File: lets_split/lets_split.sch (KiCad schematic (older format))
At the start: 60 parts, among them J1 3PIN, J2 6PIN, J3 3PIN, SW1 SW_PUSH, SW10 SW_PUSH, SW11 SW_PUSH, SW12 SW_PUSH, SW13 SW_PUSH, SW14 SW_PUSH, SW15 SW_PUSH, SW16 SW_PUSH, SW17 SW_PUSH, SW18 SW_PUSH, SW19 SW_PUSH, SW2 SW_PUSH, SW20 SW_PUSH, SW21 SW_PUSH, SW22 SW_PUSH, SW23 SW_PUSH, SW24 SW_PUSH, SW3 SW_PUSH, SW4 SW_PUSH, SW5 SW_PUSH, SW6 SW_PUSH, SW7 SW_PUSH, SW8 SW_PUSH, SW9 SW_PUSH, U1 TEENSY2.0, U2 HOLE, U3 HOLE, U4 HOLE, U5 HOLE

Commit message: Changed to use kailh sockets, start of branch
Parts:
- removed U2, U3, U4, U5: HOLE, prettylib:HOLE, symbol HOLE
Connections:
- wire segments 24 -> 57
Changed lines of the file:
@@
 LIBS:contrib
 LIBS:valves
-LIBS:component
 LIBS:lets_split-cache
 EELAYER 25 0
@@
 $EndComp
 Wire Wire Line
-	5750 2500 9450 2500
+	5750 2500 6500 2500
+Wire Wire Line
+	6500 2500 7200 2500
+Wire Wire Line
+	7200 2500 7950 2500
+Wire Wire Line
+	7950 2500 8700 2500
+Wire Wire Line
+	8700 2500 9450 2500
 Connection ~ 8700 2500
 Connection ~ 7950 2500
@@
 $EndComp
 Wire Wire Line
-	5750 3000 9450 3000
+	5750 3000 6500 3000
+Wire Wire Line
+	6500 3000 7200 3000
+Wire Wire Line
+	7200 3000 7950 3000
+Wire Wire Line
+	7950 3000 8700 3000
+Wire Wire Line
+	8700 3000 9450 3000
 Connection ~ 8700 3000
 Connection ~ 7950 3000
@@
 $EndComp
 Wire Wire Line
-	5750 3500 9450 3500
+	5750 3500 6500 3500
+Wire Wire Line
+	6500 3500 7200 3500
+Wire Wire Line
+	7200 3500 7950 3500
+Wire Wire Line
+	7950 3500 8700 3500
+Wire Wire Line
+	8700 3500 9450 3500
 Connection ~ 8700 3500
 Connection ~ 7950 3500
@@
 $EndComp
 Wire Wire Line
-	5750 4000 9450 4000
+	5750 4000 6500 4000
+Wire Wire Line
+	6500 4000 7200 4000
+Wire Wire Line
+	7200 4000 7950 4000
+Wire Wire Line
+	7950 4000 8700 4000
+Wire Wire Line
+	8700 4000 9450 4000
 Connection ~ 8700 4000
 Connection ~ 7950 4000
@@
 Connection ~ 6500 4000
 Wire Wire Line
-	5150 2200 5150 3700
+	5150 2200 5150 2700
+Wire Wire Line
+	5150 2700 5150 3200
+Wire Wire Line
+	5150 3200 5150 3700
 Connection ~ 5150 2700
 Connection ~ 5150 3200
 Wire Wire Line
-	5900 2200 5900 3700
+	5900 2200 5900 2700
+Wire Wire Line
+	5900 2700 5900 3200
+Wire Wire Line
+	5900 3200 5900 3700
 Connection ~ 5900 2700
 Connection ~ 5900 3200
 Wire Wire Line
-	6600 2200 6600 3700
+	6600 2200 6600 2700
+Wire Wire Line
+	6600 2700 6600 3200
+Wire Wire Line
+	6600 3200 6600 3700
 Connection ~ 6600 3200
 Connection ~ 6600 2700
 Wire Wire Line
-	7350 2200 7350 3700
+	7350 2200 7350 2700
+Wire Wire Line
+	7350 2700 7350 3200
+Wire Wire Line
+	7350 3200 7350 3700
 Connection ~ 7350 2700
 Connection ~ 7350 3200
 Wire Wire Line
-	8100 2200 8100 3700
+	8100 2200 8100 2700
+Wire Wire Line
+	8100 2700 8100 3200
+Wire Wire Line
+	8100 3200 8100 3700
 Connection ~ 8100 3200
 Connection ~ 8100 2700
 Wire Wire Line
-	8850 2200 8850 3700
+	8850 2200 8850 2700
+Wire Wire Line
+	8850 2700 8850 3200
+Wire Wire Line
+	8850 3200 8850 3700
 Connection ~ 8850 2700
 Connection ~ 8850 3200
@@
 Text GLabel 2600 4150 2    60   Input ~ 0
 data
-Text GLabel 6450 950  1    60   Input ~ 0
+Text GLabel 6500 900  1    55   Input ~ 0
 data
 $Comp
 L R R2
 U 1 1 57D4D4E2
-P 6300 950
-F 0 "R2" V 6380 950 50  0000 C CNN
-F 1 "R" V 6300 950 50  0000 C CNN
-F 2 "footprint:RESISTOR" V 6230 950 50  0001 C CNN
-F 3 "" H 6300 950 50  0000 C CNN
-	1    6300 950
+P 6250 950
+F 0 "R2" V 6330 950 50  0000 C CNN
+F 1 "R" V 6250 950 50  0000 C CNN
+F 2 "footprint:RESISTOR" V 6180 950 50  0001 C CNN
+F 3 "" H 6250 950 50  0000 C CNN
+	1    6250 950
 	0    1    1    0
 $EndComp
 Wire Wire Line
-	6450 950  6500 1450
-Wire Wire Line
-	6450 950  6900 950
+	6500 900  6500 950
+Wire Wire Line
+	6500 950  6500 1450
+Wire Wire Line
+	6400 950  6500 950
+Wire Wire Line
+	6500 950  6900 950
 Wire Wire Line
 	6900 950  6900 1450
-Connection ~ 6900 950
-Connection ~ 6450 950
+Connection ~ 6500 950
 Wire Wire Line
 	6800 1450 6800 1350
@@
 	6800 1350 6600 1350
 Wire Wire Line
+	6600 900  6600 1350
+Wire Wire Line
 	6600 1350 6600 1450
-Connection ~ 6800 1350
 Connection ~ 6600 1350
-Text GLabel 6600 1350 1    60   Input ~ 0
+Text GLabel 6600 900  1    55   Input ~ 0
 xtradata
 $Comp
@@
 Text GLabel 7950 950  0    60   Input ~ 0
 xtradata
-Text GLabel 4200 900  0    60   Input ~ 0
+Text GLabel 3625 3550 2    60   Input ~ 0
 xtradata
 $Comp
 L TEST W1
 U 1 1 57D52188
-P 4400 900
-F 0 "W1" H 4400 960 50  0000 C CNN
-F 1 "TEST" H 4400 830 50  0000 C CNN
-F 2 "prettylib:JUMPER_SMD_2DUB" H 4400 900 50  0001 C CNN
-F 3 "" H 4400 900 50  0000 C CNN
-	1    4400 900
-	1    0    0    -1
+P 3425 3550
+F 0 "W1" H 3425 3610 50  0000 C CNN
+F 1 "TEST" H 3425 3480 50  0000 C CNN
+F 2 "prettylib:JUMPER_SMD_2DUB" H 3425 3550 50  0001 C CNN
+F 3 "" H 3425 3550 50  0000 C CNN
+	1    3425 3550
+	-1   0    0    -1
 $EndComp
 $Comp
 L R R1
 U 1 1 57D527EC
-P 4600 750
-F 0 "R1" V 4680 750 50  0000 C CNN
-F 1 "R" V 4600 750 50  0000 C CNN
-F 2 "footprint:RESISTOR" V 4530 750 50  0001 C CNN
-F 3 "" H 4600 750 50  0000 C CNN
-	1    4600 750
+P 3175 3350
+F 0 "R1" V 3255 3350 50  0000 C CNN
+F 1 "R" V 3175 3350 50  0000 C CNN
+F 2 "footprint:RESISTOR" V 3105 3350 50  0001 C CNN
+F 3 "" H 3175 3350 50  0000 C CNN
+	1    3175 3350
 	1    0    0    -1
 $EndComp
@@
 L VCC #PWR05
 U 1 1 57D5288F
-P 6150 950
-F 0 "#PWR05" H 6150 800 50  0001 C CNN
-F 1 "VCC" H 6150 1100 50  0000 C CNN
-F 2 "" H 6150 950 50  0000 C CNN
-F 3 "" H 6150 950 50  0000 C CNN
-	1    6150 950
+P 6100 950
+F 0 "#PWR05" H 6100 800 50  0001 C CNN
+F 1 "VCC" H 6100 1100 50  0000 C CNN
+F 2 "" H 6100 950 50  0000 C CNN
+F 3 "" H 6100 950 50  0000 C CNN
+	1    6100 950
 	1    0    0    -1
 $EndComp
@@
 L VCC #PWR06
 U 1 1 57D52913
-P 4600 600
-F 0 "#PWR06" H 4600 450 50  0001 C CNN
-F 1 "VCC" H 4600 750 50  0000 C CNN
-F 2 "" H 4600 600 50  0000 C CNN
-F 3 "" H 4600 600 50  0000 C CNN
-	1    4600 600
+P 3175 3200
+F 0 "#PWR06" H 3175 3050 50  0001 C CNN
+F 1 "VCC" H 3175 3350 50  0000 C CNN
+F 2 "" H 3175 3200 50  0000 C CNN
+F 3 "" H 3175 3200 50  0000 C CNN
+	1    3175 3200
 	0    1    1    0
 $EndComp
 Wire Wire Line
-	4600 900  4600 4050
-Wire Wire Line
-	4600 4050 2600 4050
+	3175 3500 3175 3550
+Wire Wire Line
+	3175 3550 3175 4050
+Wire Wire Line
+	3175 4050 2600 4050
 Text GLabel 2600 2750 2    60   Input ~ 0
 col0
@@
 Text GLabel 5750 4000 0    60   Input ~ 0
 row3
-$Comp
-L HOLE U2
-U 1 1 57D4E136
-P 1950 6500
-F 0 "U2" H 1950 6500 60  0000 C CNN
-F 1 "HOLE" H 1950 6500 60  0000 C CNN
-F 2 "prettylib:HOLE" H 1950 6500 60  0001 C CNN
-F 3 "" H 1950 6500 60  0000 C CNN
-	1    1950 6500
-	1    0    0    -1
-$EndComp
-$Comp
-L HOLE U3
-U 1 1 57D4E261
-P 4050 6500
-F 0 "U3" H 4050 6500 60  0000 C CNN
-F 1 "HOLE" H 4050 6500 60  0000 C CNN
-F 2 "prettylib:HOLE" H 4050 6500 60  0001 C CNN
-F 3 "" H 4050 6500 60  0000 C CNN
-	1    4050 6500
-	1    0    0    -1
-$EndComp
-$Comp
-L HOLE U4
-U 1 1 57D4E2F6
-P 6050 5650
-F 0 "U4" H 6050 5650 60  0000 C CNN
-F 1 "HOLE" H 6050 5650 60  0000 C CNN
-F 2 "prettylib:HOLE" H 6050 5650 60  0001 C CNN
-F 3 "" H 6050 5650 60  0000 C CNN
-	1    6050 5650
-	1    0    0    -1
-$EndComp
-$Comp
-L HOLE U5
-U 1 1 57D4E38F
-P 8600 5650
-F 0 "U5" H 8600 5650 60  0000 C CNN
-F 1 "HOLE" H 8600 5650 60  0000 C CNN
-F 2 "prettylib:HOLE" H 8600 5650 60  0001 C CNN
-F 3 "" H 8600 5650 60  0000 C CNN
-	1    8600 5650
-	1    0    0    -1
-$EndComp
+Wire Wire Line
+	3225 3550 3175 3550
+Connection ~ 3175 3550
 $EndSCHEMATC

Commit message: Finished desing
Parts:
- removed J2: 6PIN, footprint:4pin35mmAudio, symbol 6PIN
- removed R1, R2: R, footprint:RESISTOR, symbol R
- removed U1: TEENSY2.0, footprint:TEENSY_2.0, symbol TEENSY2.0
- removed W1: TEST, prettylib:JUMPER_SMD_2DUB, symbol TEST
- removed W2: TEST_1P, Wire_Pads:SolderWirePad_single_2mmDrill, symbol TEST_1P
- added J2: CONN_01X04, Connectors:4ucon-20153, symbol CONN_01X04
- added JP1: I2C / Serial, Jumpers:Solder-jumper-NO, symbol JUMPER
- added R1, R2: 4k7, Resistors_ThroughHole:R_Axial_DIN0207_L6.3mm_D2.5mm_P10.16mm_Horizontal, symbol R_Small
- added U1: ArduinoProMicro, plug-in-modules:ArduinoProMicro, symbol ArduinoProMicro
- J1, J3: footprint prettylib:jumper -> Jumpers:jumper-3pin-smd-dualside
- SW1, SW24: footprint flipalps:MXALPS_FLIP -> CherryMX:Kailh-socket
- SW10: renamed from SW14; footprint flipalps:MXALPS_FLIP -> CherryMX:Kailh-socket
- SW11: renamed from SW18; footprint flipalps:MXALPS_FLIP -> CherryMX:Kailh-socket
- SW12: renamed from SW22; footprint flipalps:MXALPS_FLIP -> CherryMX:Kailh-socket
- SW13: renamed from SW3; footprint flipalps:MXALPS_FLIP -> CherryMX:Kailh-socket
- SW14: renamed from SW7; footprint flipalps:MXALPS_FLIP -> CherryMX:Kailh-socket
- SW15: renamed from SW11; footprint flipalps:MXALPS_FLIP -> CherryMX:Kailh-socket
- SW16: renamed from SW15; footprint flipalps:MXALPS_FLIP -> CherryMX:Kailh-socket
- SW17: renamed from SW19; footprint flipalps:MXALPS_FLIP -> CherryMX:Kailh-socket
- SW18: renamed from SW23; footprint flipalps:MXALPS_FLIP -> CherryMX:Kailh-socket
- SW19: renamed from SW4; footprint flipalps:MXALPS_FLIP -> CherryMX:Kailh-socket
- SW2: renamed from SW5; footprint flipalps:MXALPS_FLIP -> CherryMX:Kailh-socket
- SW20: renamed from SW8; footprint flipalps:MXALPS_FLIP -> CherryMX:Kailh-socket
- SW21: renamed from SW12; footprint flipalps:MXALPS_FLIP -> CherryMX:Kailh-socket
- SW22: renamed from SW16; footprint flipalps:MXALPS_FLIP -> CherryMX:Kailh-socket
- SW23: renamed from SW20; footprint flipalps:MXALPS_FLIP -> CherryMX:Kailh-socket
- SW3: renamed from SW9; footprint flipalps:MXALPS_FLIP -> CherryMX:Kailh-socket
- SW4: renamed from SW13; footprint flipalps:MXALPS_FLIP -> CherryMX:Kailh-socket
- SW5: renamed from SW17; footprint flipalps:MXALPS_FLIP -> CherryMX:Kailh-socket
- SW6: renamed from SW21; footprint flipalps:MXALPS_FLIP -> CherryMX:Kailh-socket
- SW7: renamed from SW2; footprint flipalps:MXALPS_FLIP -> CherryMX:Kailh-socket
- SW8: renamed from SW6; footprint flipalps:MXALPS_FLIP -> CherryMX:Kailh-socket
- SW9: renamed from SW10; footprint flipalps:MXALPS_FLIP -> CherryMX:Kailh-socket
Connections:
- net labels added: SCL/D3, SDA
- net labels removed: data, xtradata
- wire segments 57 -> 30

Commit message: Moved panel files into subfolder
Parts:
- removed J1, J3: 3PIN, Jumpers:jumper-3pin-smd-dualside, symbol 3PIN
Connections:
- wire segments 30 -> 61
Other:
- moved on the sheet: J2
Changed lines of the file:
@@
-$EndComp
-$Comp
-L 3PIN J1
-U 1 1 57D4A05A
-P 5750 1700
-F 0 "J1" H 5700 1900 60  0000 C CNN
-F 1 "3PIN" H 5700 1500 60  0000 C CNN
-F 2 "Jumpers:jumper-3pin-smd-dualside" H 5750 1700 60  0001 C CNN
-F 3 "" H 5750 1700 60  0000 C CNN
-	1    5750 1700
-	0    -1   -1   0
-$EndComp
-$Comp
-L 3PIN J3
-U 1 1 57D4A13F
-P 7450 1700
-F 0 "J3" H 7400 1900 60  0000 C CNN
-F 1 "3PIN" H 7400 1500 60  0000 C CNN
-F 2 "Jumpers:jumper-3pin-smd-dualside" H 7450 1700 60  0001 C CNN
-F 3 "" H 7450 1700 60  0000 C CNN
-	1    7450 1700
-	0    -1   -1   0
 $EndComp
 $Comp
 L VCC #PWR01
 U 1 1 57D4A6E4
-P 7550 1500
-F 0 "#PWR01" H 7550 1350 50  0001 C CNN
-F 1 "VCC" H 7550 1650 50  0000 C CNN
-F 2 "" H 7550 1500 50  0000 C CNN
-F 3 "" H 7550 1500 50  0000 C CNN
-	1    7550 1500
-	1    0    0    -1
-$EndComp
-$Comp
-L VCC #PWR02
-U 1 1 57D4A760
-P 5850 1500
-F 0 "#PWR02" H 5850 1350 50  0001 C CNN
-F 1 "VCC" H 5850 1650 50  0000 C CNN
-F 2 "" H 5850 1500 50  0000 C CNN
-F 3 "" H 5850 1500 50  0000 C CNN
-	1    5850 1500
-	1    0    0    -1
-$EndComp
-$Comp
-L GND #PWR03
+P 5850 1325
+F 0 "#PWR01" H 5850 1175 50  0001 C CNN
+F 1 "VCC" H 5850 1475 50  0000 C CNN
+F 2 "" H 5850 1325 50  0000 C CNN
+F 3 "" H 5850 1325 50  0000 C CNN
+	1    5850 1325
+	1    0    0    -1
+$EndComp
+$Comp
+L GND #PWR02
 U 1 1 57D4A7DC
-P 5650 1500
-F 0 "#PWR03" H 5650 1250 50  0001 C CNN
-F 1 "GND" H 5650 1350 50  0000 C CNN
-F 2 "" H 5650 1500 50  0000 C CNN
-F 3 "" H 5650 1500 50  0000 C CNN
-	1    5650 1500
-	-1   0    0    1
-$EndComp
-$Comp
-L GND #PWR04
-U 1 1 57D4A858
-P 7350 1500
-F 0 "#PWR04" H 7350 1250 50  0001 C CNN
-F 1 "GND" H 7350 1350 50  0000 C CNN
-F 2 "" H 7350 1500 50  0000 C CNN
-F 3 "" H 7350 1500 50  0000 C CNN
-	1    7350 1500
-	-1   0    0    1
+P 6325 1525
+F 0 "#PWR02" H 6325 1275 50  0001 C CNN
+F 1 "GND" H 6325 1375 50  0000 C CNN
+F 2 "" H 6325 1525 50  0000 C CNN
+F 3 "" H 6325 1525 50  0000 C CNN
+	1    6325 1525
+	1    0    0    -1
 $EndComp
 Text GLabel 2350 2375 2    55   Input ~ 0
@@
 row0
 $Comp
-L VCC #PWR05
+L VCC #PWR03
 U 1 1 57D5E2B3
 P 1400 1900
-F 0 "#PWR05" H 1400 1750 50  0001 C CNN
+F 0 "#PWR03" H 1400 1750 50  0001 C CNN
 F 1 "VCC" H 1400 2050 50  0000 C CNN
 F 2 "" H 1400 1900 50  0000 C CNN
@@
 $EndComp
 $Comp
-L GND #PWR06
+L GND #PWR04
 U 1 1 57D5FCCF
 P 1400 3050
-F 0 "#PWR06" H 1400 2800 50  0001 C CNN
+F 0 "#PWR04" H 1400 2800 50  0001 C CNN
 F 1 "GND" H 1400 2900 50  0000 C CNN
 F 2 "" H 1400 3050 50  0000 C CNN
@@
 L CONN_01X04 J2
 U 1 1 59DC675D
-P 6550 1650
-F 0 "J2" H 6550 1900 50  0000 C CNN
-F 1 "CONN_01X04" V 6650 1650 50  0000 C CNN
-F 2 "Connectors:4ucon-20153" H 6550 1650 50  0001 C CNN
-F 3 "" H 6550 1650 50  0000 C CNN
-	1    6550 1650
-	0    -1   1    0
+P 6575 1325
+F 0 "J2" H 6575 1575 50  0000 C CNN
+F 1 "CONN_01X04" V 6675 1325 50  0000 C CNN
+F 2 "Connectors:4ucon-20153" H 6575 1325 50  0001 C CNN
+F 3 "" H 6575 1325 50  0000 C CNN
+	1    6575 1325
+	1    0    0    1
 $EndComp
 $Comp
@@
 $EndComp
 Wire Wire Line
-	5750 2500 9450 2500
+	5750 2500 6500 2500
+Wire Wire Line
+	6500 2500 7200 2500
+Wire Wire Line
+	7200 2500 7950 2500
+Wire Wire Line
+	7950 2500 8700 2500
+Wire Wire Line
+	8700 2500 9450 2500
 Connection ~ 8700 2500
 Connection ~ 7950 2500
@@
 Connection ~ 6500 2500
 Wire Wire Line
-	5750 3000 9450 3000
+	5750 3000 6500 3000
+Wire Wire Line
+	6500 3000 7200 3000
+Wire Wire Line
+	7200 3000 7950 3000
+Wire Wire Line
+	7950 3000 8700 3000
+Wire Wire Line
+	8700 3000 9450 3000
 Connection ~ 8700 3000
 Connection ~ 7950 3000
@@
 Connection ~ 6500 3000
 Wire Wire Line
-	5750 3500 9450 3500
+	5750 3500 6500 3500
+Wire Wire Line
+	6500 3500 7200 3500
+Wire Wire Line
+	7200 3500 7950 3500
+Wire Wire Line
+	7950 3500 8700 3500
+Wire Wire Line
+	8700 3500 9450 3500
 Connection ~ 8700 3500
 Connection ~ 7950 3500
@@
 Connection ~ 6500 3500
 Wire Wire Line
-	5750 4000 9450 4000
+	5750 4000 6500 4000
+Wire Wire Line
+	6500 4000 7200 4000
+Wire Wire Line
+	7200 4000 7950 4000
+Wire Wire Line
+	7950 4000 8700 4000
+Wire Wire Line
+	8700 4000 9450 4000
 Connection ~ 8700 4000
 Connection ~ 7950 4000
@@
 Connection ~ 6500 4000
 Wire Wire Line
-	5150 2200 5150 3700
+	5150 2200 5150 2700
+Wire Wire Line
+	5150 2700 5150 3200
+Wire Wire Line
+	5150 3200 5150 3700
 Connection ~ 5150 2700
 Connection ~ 5150 3200
 Wire Wire Line
-	5900 2200 5900 3700
+	5900 2200 5900 2700
+Wire Wire Line
+	5900 2700 5900 3200
+Wire Wire Line
+	5900 3200 5900 3700
 Connection ~ 5900 2700
 Connection ~ 5900 3200
 Wire Wire Line
-	6600 2200 6600 3700
+	6600 2200 6600 2700
+Wire Wire Line
+	6600 2700 6600 3200
+Wire Wire Line
+	6600 3200 6600 3700
 Connection ~ 6600 3200
 Connection ~ 6600 2700
 Wire Wire Line
-	7350 2200 7350 3700
+	7350 2200 7350 2700
+Wire Wire Line
+	7350 2700 7350 3200
+Wire Wire Line
+	7350 3200 7350 3700
 Connection ~ 7350 2700
 Connection ~ 7350 3200
 Wire Wire Line
-	8100 2200 8100 3700
+	8100 2200 8100 2700
+Wire Wire Line
+	8100 2700 8100 3200
+Wire Wire Line
+	8100 3200 8100 3700
 Connection ~ 8100 3200
 Connection ~ 8100 2700
 Wire Wire Line
-	8850 2200 8850 3700
+	8850 2200 8850 2700
+Wire Wire Line
+	8850 2700 8850 3200
+Wire Wire Line
+	8850 3200 8850 3700
 Connection ~ 8850 2700
 Connection ~ 8850 3200
 Wire Wire Line
-	7450 1500 7450 1200
-Wire Wire Line
-	7450 1200 6700 1200
-Wire Wire Line
-	6700 1200 6700 1450
-Wire Wire Line
-	5750 1500 5750 1150
-Wire Wire Line
-	5750 1150 6400 1150
-Wire Wire Line
-	6400 1150 6400 1450
-Wire Wire Line
-	1400 2750 1400 3050
+	5850 1375 6375 1375
+Wire Wire Line
+	1400 2750 1400 2850
+Wire Wire Line
+	1400 2850 1400 2950
+Wire Wire Line
+	1400 2950 1400 3050
 Wire Wire Line
 	1400 2950 1550 2950
@@
 $EndComp
 Wire Wire Line
-	2350 2075 2850 2075
+	2350 2075 2750 2075
+Wire Wire Line
+	2750 2075 2850 2075
 Wire Wire Line
 	2750 2075 2750 1925
 Wire Wire Line
-	2350 1975 2850 1975
+	2350 1975 2650 1975
+Wire Wire Line
+	2650 1975 2850 1975
 Wire Wire Line
 	2650 1975 2650 1925
@@
 	2650 1725 2650 1675
 Wire Wire Line
-	2650 1675 2750 1675
+	2650 1675 2700 1675
+Wire Wire Line
+	2700 1675 2750 1675
 Wire Wire Line
 	2750 1675 2750 1725
@@
 Connection ~ 2700 1675
 $Comp
-L VCC #PWR07
+L VCC #PWR05
 U 1 1 59DCE20A
 P 2700 1000
-F 0 "#PWR07" H 2700 850 50  0001 C CNN
+F 0 "#PWR05" H 2700 850 50  0001 C CNN
 F 1 "VCC" H 2700 1150 50  0000 C CNN
 F 2 "" H 2700 1000 50  0000 C CNN
@@
 Text GLabel 2850 2075 2    55   Input ~ 0
 SCL/D3
-Text GLabel 6500 1450 1    55   Input ~ 0
+Text GLabel 6375 1275 0    55   Input ~ 0
 SCL/D3
-Text GLabel 6600 1450 1    55   Input ~ 0
+Text GLabel 6375 1175 0    55   Input ~ 0
 SDA
+Wire Wire Line
+	6325 1525 6325 1475
+Wire Wire Line
+	6325 1475 6375 1475
+Wire Wire Line
+	5850 1325 5850 1375
 $EndSCHEMATC

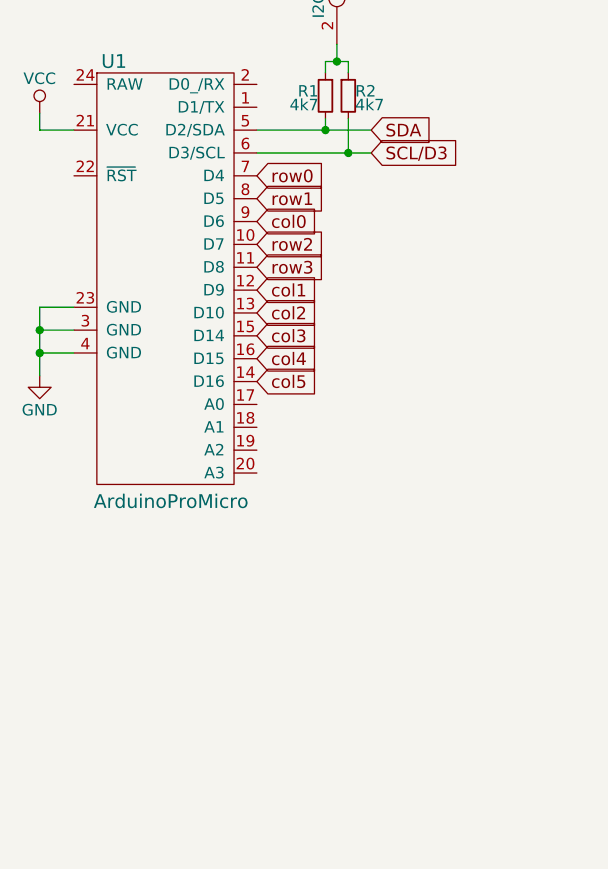
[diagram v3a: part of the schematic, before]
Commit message: V3 version, with mini usb added
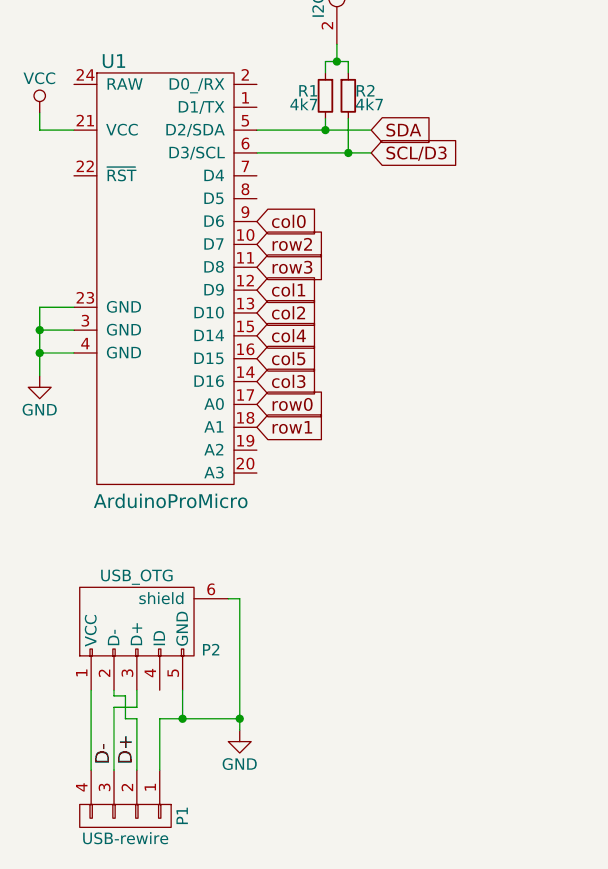
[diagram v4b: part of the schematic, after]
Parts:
- added P1: USB-rewire, Pin_Headers:Pin_Header_Straight_1x04_Pitch2.00mm, symbol CONN_01X04
- added P2: USB_OTG, Connectors:USB-Mini-B-SMD, symbol USB_OTG
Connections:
- net GND: now also P1.1 (P1), P2.5 (GND), P2.6 (shield)
- net col3: now also U1.14 (D16); no longer U1.15 (D14)
- net col4: now also U1.15 (D14); no longer U1.16 (D15)
- net col5: now also U1.16 (D15); no longer U1.14 (D16)
- net row0: now also U1.17 (A0); no longer U1.7 (D4)
- net row1: now also U1.18 (A1); no longer U1.8 (D5)
- new net: P1.4 (P4), P2.1 (VCC)
- new net D+: P1.2 (P2), P2.2 (D-)
- new net D-: P1.3 (P3), P2.3 (D+)
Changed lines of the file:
@@
 Text GLabel 2350 2775 2    55   Input ~ 0
 col2
+Text GLabel 2350 3075 2    55   Input ~ 0
+col3
 Text GLabel 2350 2875 2    55   Input ~ 0
-col3
+col4
 Text GLabel 2350 2975 2    55   Input ~ 0
-col4
-Text GLabel 2350 3075 2    55   Input ~ 0
 col5
 Text GLabel 2350 2575 2    55   Input ~ 0
@@
 Text GLabel 2350 2475 2    55   Input ~ 0
 row2
-Text GLabel 2350 2275 2    55   Input ~ 0
+Text GLabel 2350 3275 2    55   Input ~ 0
 row1
-Text GLabel 2350 2175 2    55   Input ~ 0
+Text GLabel 2350 3175 2    55   Input ~ 0
 row0
 $Comp
@@
 Wire Wire Line
 	5850 1325 5850 1375
+$Comp
+L CONN_01X04 P1
+U 1 1 59DD2CD9
+P 1775 4975
+F 0 "P1" H 1775 5225 50  0000 C CNN
+F 1 "USB-rewire" V 1875 4975 50  0000 C CNN
+F 2 "Pin_Headers:Pin_Header_Straight_1x04_Pitch2.00mm" H 1775 4975 50  0001 C CNN
+F 3 "" H 1775 4975 50  0000 C CNN
+	1    1775 4975
+	0    1    1    0
+$EndComp
+Wire Wire Line
+	2225 4025 2275 4025
+Wire Wire Line
+	2275 4025 2275 4550
+Wire Wire Line
+	2275 4550 2275 4600
+Wire Wire Line
+	1925 4550 2025 4550
+Wire Wire Line
+	2025 4550 2275 4550
+Wire Wire Line
+	2025 4550 2025 4425
+Connection ~ 2025 4550
+$Comp
+L GND #PWR06
+U 1 1 59DD4C5E
+P 2275 4600
+F 0 "#PWR06" H 2275 4350 50  0001 C CNN
+F 1 "GND" H 2275 4450 50  0000 C CNN
+F 2 "" H 2275 4600 50  0000 C CNN
+F 3 "" H 2275 4600 50  0000 C CNN
+	1    2275 4600
+	1    0    0    -1
+$EndComp
+Connection ~ 2275 4550
+$Comp
+L USB_OTG P2
+U 1 1 59DD5ACB
+P 1825 4125
+F 0 "P2" H 2150 4000 50  0000 C CNN
+F 1 "USB_OTG" H 1825 4325 50  0000 C CNN
+F 2 "Connectors:USB-Mini-B-SMD" V 1775 4025 50  0001 C CNN
+F 3 "" V 1775 4025 50  0000 C CNN
+	1    1825 4125
+	1    0    0    -1
+$EndComp
+Wire Wire Line
+	1625 4425 1625 4775
+Wire Wire Line
+	1925 4775 1925 4550
+Text Label 1725 4750 1    60   ~ 0
+D-
+Text Label 1825 4750 1    60   ~ 0
+D+
+Wire Wire Line
+	1725 4500 1725 4775
+Wire Wire Line
+	1725 4500 1825 4500
+Wire Wire Line
+	1825 4500 1825 4425
+Wire Wire Line
+	1825 4550 1825 4775
+Wire Wire Line
+	1825 4550 1775 4550
+Wire Wire Line
+	1775 4550 1775 4450
+Wire Wire Line
+	1775 4450 1725 4450
+Wire Wire Line
+	1725 4450 1725 4425
 $EndSCHEMATC
